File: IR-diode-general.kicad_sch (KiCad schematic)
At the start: 32 parts, among them J1 BarrelJack_3167288, J2 USB4105-GF-A, U1 MP2483DQ-LF-P, U2 AP62301Z6-7

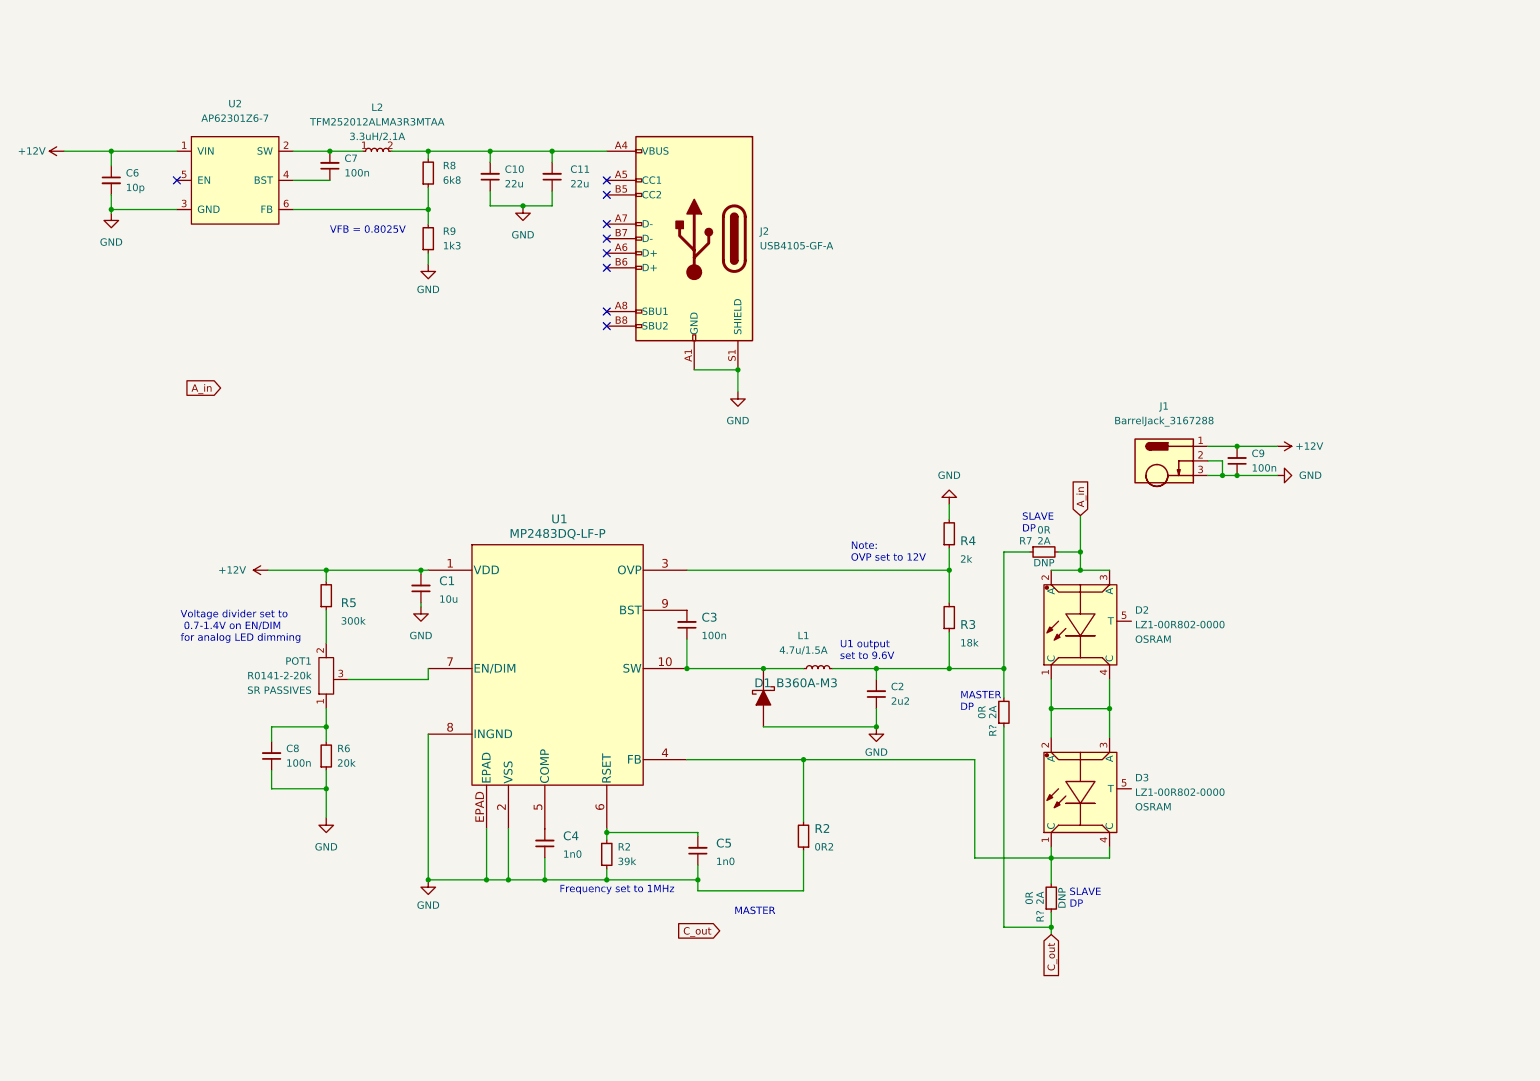
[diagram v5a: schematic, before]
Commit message: Introduced hierarchical schematics
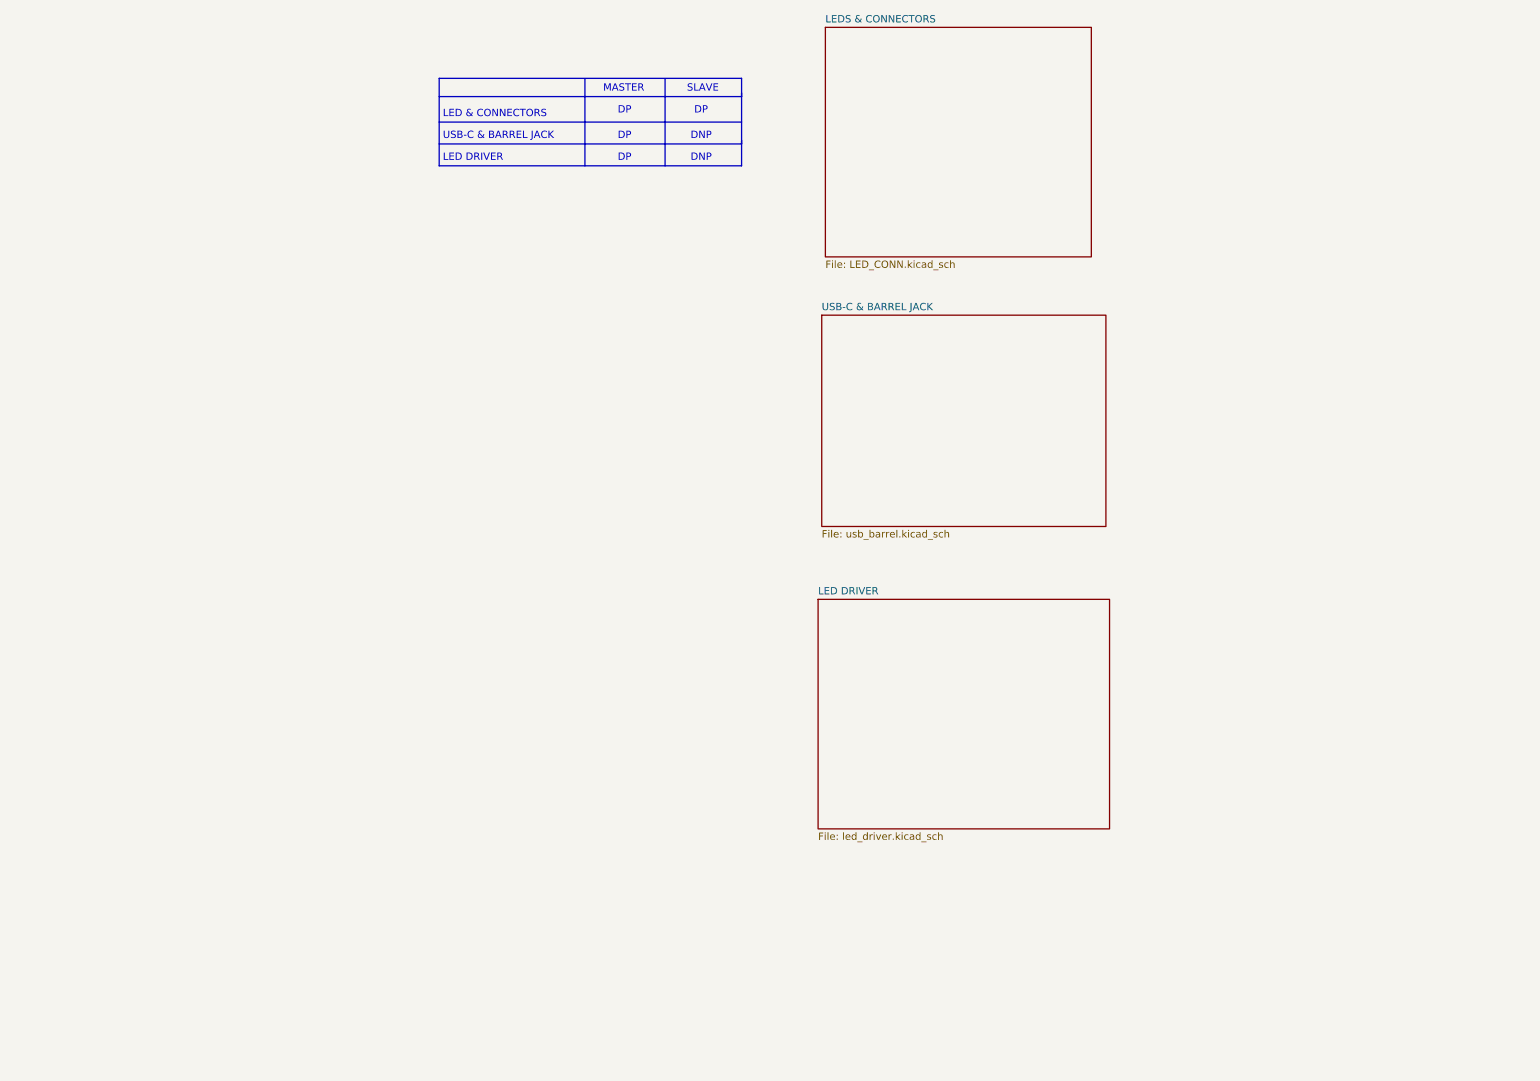
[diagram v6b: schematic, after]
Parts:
- removed C1: C_10u_0805, antmicro-footprints:0805-cap, symbol antmicroCapacitorsmisc:C_10u_0805
- removed C10, C11: C_22u_0603, antmicro-footprints:C_0603_1608Metric, symbol antmicroCapacitors0603:C_22u_0603
- removed C2: C_2u2_0603, antmicro-footprints:0603-cap, symbol antmicroCapacitors0603:C_2u2_0603
- removed C3, C7, C8, C9: C_100n_0402, antmicro-footprints:C_0402_1005Metric, symbol antmicroCapacitors0402:C_100n_0402
- removed C4, C5: C_1n0_0402, antmicro-footprints:0402-cap, symbol antmicroCapacitors0402:C_1n0_0402
- removed C6: C_10p_0402, antmicro-footprints:C_0402_1005Metric, symbol antmicroCapacitors0402:C_10p_0402
- removed D1: B360A-M3, antmicro-footprints:DO-214AC, symbol antmicroDiodesRectifiersSingle:B360A-M3
- removed D2, D3: LZ1-00R802-0000, antmicro-footprints:LZ1-00R802_4EP_4.4x4.4, symbol antmicroLEDIndicationDiscrete:LZ1-00R802-0000
- removed J1: BarrelJack_3167288, antmicro-footprints:BarrelJack_3167288_Horizontal, symbol antmicroBarrelAudioConnectors:BarrelJack_3167288
- removed J2: USB4105-GF-A, antmicro-footprints:GCT_USB4105-GF-A, symbol antmicroUSBDVIHDMIConnectors:USB4105-GF-A
- removed L1: SRP2512A-4R7M, antmicro-footprints:SRP2512A-1R0M, symbol antmicroFixedInductors:SRP2512A-4R7M
- removed L2: TFM252012ALMA3R3MTAA, antmicro-footprints:L_1008_2520Metric, symbol antmicroFixedInductors:TFM252012ALMA3R3MTAA
- removed POT1: R0141-2-20k, antmicro-footprints:R0141-2-20k, symbol antmicroRotaryPotentiometersRheostats:R0141-2-20k
- removed R2: R_0R2_1206, antmicro-footprints:1206-res, symbol antmicroResistorsmisc:R_0R2_1206
- removed R2: R_39k_0402, antmicro-footprints:0402-res, symbol antmicroResistors0402:R_39k_0402
- removed R3: R_18k_0402, antmicro-footprints:0402-res, symbol antmicroResistors0402:R_18k_0402
- removed R4: R_2k_0402, antmicro-footprints:R_0402_1005Metric, symbol antmicroResistors0402:R_2k_0402
- removed R5: R_300k_0603, antmicro-footprints:0603-res, symbol antmicroResistors0603:R_300k_0603
- removed R6: R_20k_0402, antmicro-footprints:R_0402_1005Metric, symbol antmicroResistors0402:R_20k_0402
- removed R7, R? (x2): R_0R_1206, antmicro-footprints:R_1206_3216Metric, symbol antmicroResistorsmisc:R_0R_1206
- removed R8: R_6k8_0402, antmicro-footprints:0402-res, symbol antmicroResistors0402:R_6k8_0402
- removed R9: R_1k3_0402, antmicro-footprints:R_0402_1005Metric, symbol antmicroResistors0402:R_1k3_0402
- removed U1: MP2483DQ-LF-P, antmicro-footprints:MP2483DQ-LF-P, symbol antmicroPMICLEDDrivers:MP2483DQ-LF-P
- removed U2: AP62301Z6-7, antmicro-footprints:SOT-563, symbol antmicroDCDCConverters:AP62301Z6-7
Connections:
- no-connect marks 9 -> 0
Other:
- added sheet LED DRIVER (led_driver.kicad_sch)
- added sheet LEDS & CONNECTORS (LED_CONN.kicad_sch)
- added sheet USB-C & BARREL JACK (usb_barrel.kicad_sch)
- note added: "DNP"
- note added: "DP"
- note added: "LED & CONNECTORS"
- note added: "LED DRIVER"
- note added: "SLAVE"
- note added: "USB-C & BARREL JACK"
- note removed: "Frequency set to 1MHz"
- note removed: "MASTER DP"
- note removed: "Note: OVP set to 12V"
- note removed: "SLAVE DP"
- note removed: "U1 output set to 9.6V"
- note removed: "VFB = 0.8025V"
- note removed: "Voltage divider set to 0.7-1.4V on EN/DIM for analog LED dimming"
